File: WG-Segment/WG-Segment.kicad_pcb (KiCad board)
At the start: 4 copper layers, 100 x 100 mm, 137 parts, among them J101 Conn_01x02, J102 Conn_02x04_Odd_Even, J201 Conn_01x03, J202 Conn_01x02, J203 Conn_01x04, J501 Conn_01x02, J502 Conn_01x02, J503 Conn_01x02, J504 Conn_01x02, J505 Conn_01x02, J506 Conn_01x02, J507 Conn_01x02, J508 Conn_01x02, J509 Conn_01x02, J510 Conn_01x02, J511 Conn_01x02, J512 Conn_01x02, J513 Conn_01x02, J514 Conn_01x02, J515 Conn_01x02, J516 Conn_01x02, J517 Conn_01x02, J518 Conn_01x02, J519 Conn_01x02, J520 Conn_01x02, J521 Conn_01x02, J522 Conn_01x02, J523 Conn_01x02, J524 Conn_01x02, J525 Conn_01x02, SW201 SPST-NO, U201 W25Q16JV, U202 RP2040, U301 AP63205WU, U302 MIC5504-3.3YM5, U303 MCP1501T-33E, U401 SN74LV1T34DCK, U501 SN74LV4051ADYYR, U502 SN74LV4051ADYYR, U503 SN74LV4051ADYYR, U504 SN74LV4051ADYYR, Y201 12MHz

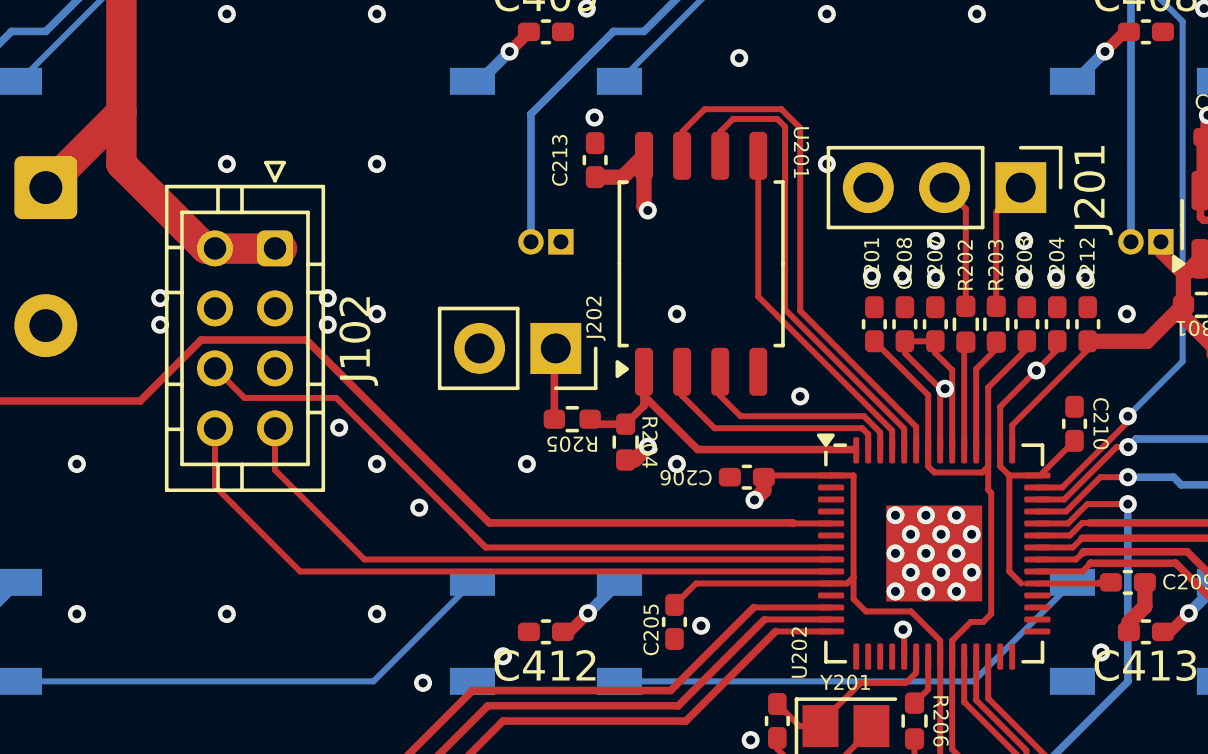
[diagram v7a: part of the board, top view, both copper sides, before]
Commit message: Minor pinout adjustments
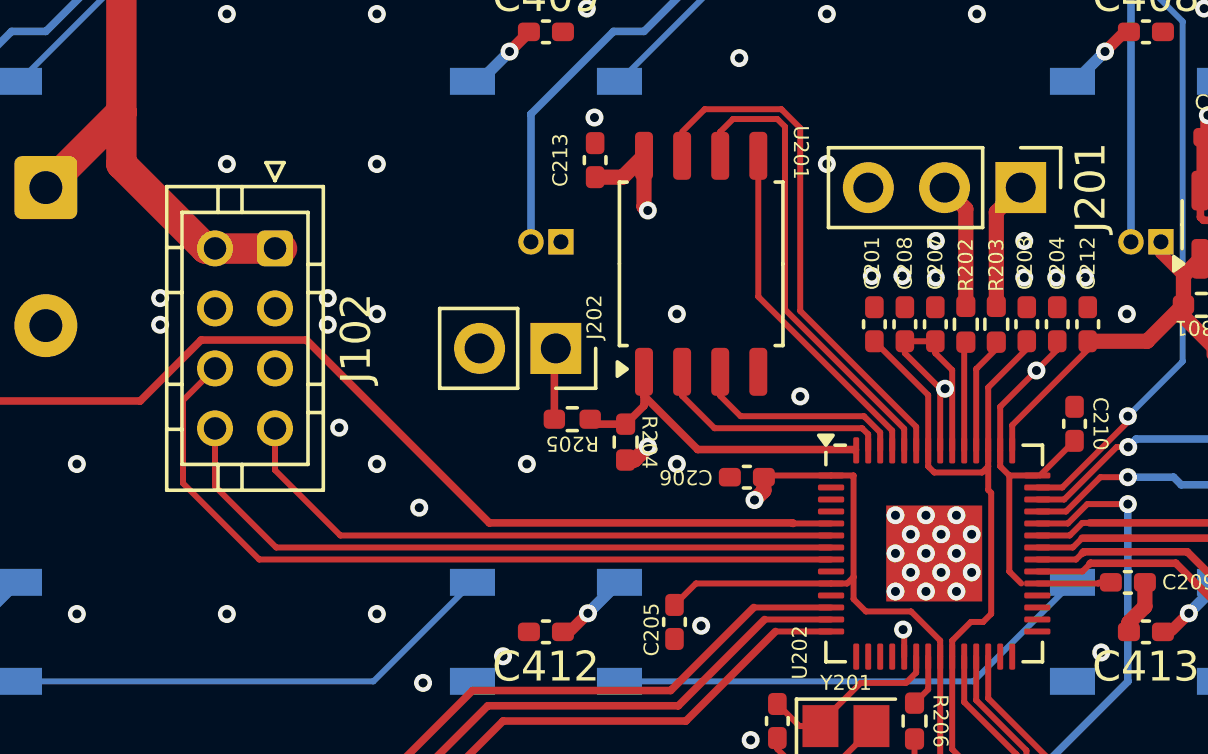
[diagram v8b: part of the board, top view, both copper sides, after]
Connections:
- U202 pad 6: unconnected-(U202-GPIO4-Pad6) -> /SDA
- U202 pad 7: /~{DS}/~{INT} -> /SCK
- U202 pad 8: /SDA -> /~{DS}/~{INT}
- U202 pad 9: /SCK -> unconnected-(U202-GPIO7-Pad9)
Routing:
- net /~{DS}/~{INT}: track 23.7 -> 26.9 mm
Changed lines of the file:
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@@
   (net 108 "unconnected-(U504-Y3-Pad12)")
   (net 109 "unconnected-(U202-GPIO21-Pad32)")
-  (net 110 "unconnected-(U202-GPIO4-Pad6)")
+  (net 110 "unconnected-(U202-GPIO7-Pad9)")
   (net 111 "unconnected-(U202-GPIO20-Pad31)")
   (net 112 "unconnected-(U202-GPIO19-Pad30)")
@@
       (net 85 "/CPU/LED_DOUT") (pinfunction "GPIO3") (pintype "bidirectional"))
     (pad "6" smd roundrect (at -3.4375 -0.6) (size 0.875 0.2) (layers "F.Cu" "F.Paste" "F.Mask") (roundrect_rratio 0.25)
-      (net 110 "unconnected-(U202-GPIO4-Pad6)") (pinfunction "GPIO4") (pintype "bidirectional+no_connect"))
+      (net 39 "/SDA") (pinfunction "GPIO4") (pintype "bidirectional"))
     (pad "7" smd roundrect (at -3.4375 -0.2) (size 0.875 0.2) (layers "F.Cu" "F.Paste" "F.Mask") (roundrect_rratio 0.25)
-      (net 38 "/~{DS}{slash}~{INT}") (pinfunction "GPIO5") (pintype "bidirectional"))
+      (net 40 "/SCK") (pinfunction "GPIO5") (pintype "bidirectional"))
     (pad "8" smd roundrect (at -3.4375 0.2) (size 0.875 0.2) (layers "F.Cu" "F.Paste" "F.Mask") (roundrect_rratio 0.25)
-      (net 39 "/SDA") (pinfunction "GPIO6") (pintype "bidirectional"))
+      (net 38 "/~{DS}{slash}~{INT}") (pinfunction "GPIO6") (pintype "bidirectional"))
     (pad "9" smd roundrect (at -3.4375 0.6) (size 0.875 0.2) (layers "F.Cu" "F.Paste" "F.Mask") (roundrect_rratio 0.25)
-      (net 40 "/SCK") (pinfunction "GPIO7") (pintype "bidirectional"))
+      (net 110 "unconnected-(U202-GPIO7-Pad9)") (pinfunction "GPIO7") (pintype "bidirectional+no_connect"))
     (pad "10" smd roundrect (at -3.4375 1) (size 0.875 0.2) (layers "F.Cu" "F.Paste" "F.Mask") (roundrect_rratio 0.25)
       (net 10 "+3V3") (pinfunction "IOVDD") (pintype "passive"))
@@
   (segment (start 181.41 139.77) (end 184.71 136.47) (width 0.2) (layer "B.Cu") (net 36))
   (segment (start 169.61 139.77) (end 181.41 139.77) (width 0.2) (layer "B.Cu") (net 36))
-  (segment (start 120.170928 90.3224) (end 117.1128 90.3224) (width 0.2) (layer "F.Cu") (net 38))
-  (segment (start 136.6645 95.3075) (end 125.156028 95.3075) (width 0.2) (layer "F.Cu") (net 38))
-  (segment (start 117.1128 90.3224) (end 117.094 90.3036) (width 0.2) (layer "F.Cu") (net 38))
-  (segment (start 125.156028 95.3075) (end 124.677664 94.829136) (width 0.2) (layer "F.Cu") (net 38))
-  (segment (start 125.149329 95.3008) (end 124.677664 94.829136) (width 0.2) (layer "F.Cu") (net 38))
-  (segment (start 117.094 90.3036) (end 116.1288 89.3384) (width 0.2) (layer "F.Cu") (net 38))
-  (segment (start 124.677664 94.829136) (end 120.170928 90.3224) (width 0.2) (layer "F.Cu") (net 38))
-  (segment (start 136.6645 95.7075) (end 121.1075 95.7075) (width 0.2) (layer "F.Cu") (net 39))
+  (segment (start 115.062 93.1672) (end 115.062 90.4052) (width 0.2) (layer "F.Cu") (net 38))
+  (segment (start 136.6645 95.7075) (end 117.6023 95.7075) (width 0.2) (layer "F.Cu") (net 38))
+  (segment (start 117.6023 95.7075) (end 115.062 93.1672) (width 0.2) (layer "F.Cu") (net 38))
+  (segment (start 115.062 90.4052) (end 116.1288 89.3384) (width 0.2) (layer "F.Cu") (net 38))
+  (segment (start 136.6645 94.9075) (end 120.3075 94.9075) (width 0.2) (layer "F.Cu") (net 39))
+  (segment (start 120.3075 94.9075) (end 118.1288 92.7288) (width 0.2) (layer "F.Cu") (net 39))
   (segment (start 118.1288 92.7288) (end 118.1288 91.3384) (width 0.2) (layer "F.Cu") (net 39))
-  (segment (start 121.1075 95.7075) (end 118.1288 92.7288) (width 0.2) (layer "F.Cu") (net 39))
-  (segment (start 136.6645 96.1075) (end 118.9675 96.1075) (width 0.2) (layer "F.Cu") (net 40))
-  (segment (start 118.9675 96.1075) (end 116.7384 93.8784) (width 0.2) (layer "F.Cu") (net 40))
+  (segment (start 118.1675 95.3075) (end 116.1288 93.2688) (width 0.2) (layer "F.Cu") (net 40))
   (segment (start 116.1288 93.2688) (end 116.1288 91.3384) (width 0.2) (layer "F.Cu") (net 40))
-  (segment (start 116.7384 93.8784) (end 116.1288 93.2688) (width 0.2) (layer "F.Cu") (net 40))
-  (segment (start 142.172 84.127) (end 142.172 87.2685) (width 0.2) (layer "F.Cu") (net 41))
-  (segment (start 142.987 83.312) (end 142.172 84.127) (width 0.2) (layer "F.Cu") (net 41))
-  (segment (start 141.156 84.021) (end 141.156 87.2685) (width 0.2) (layer "F.Cu") (net 42))
-  (segment (start 140.447 83.312) (end 141.156 84.021) (width 0.2) (layer "F.Cu") (net 42))
+  (segment (start 136.6645 95.3075) (end 118.1675 95.3075) (width 0.2) (layer "F.Cu") (net 40))
+  (segment (start 142.172 84.127) (end 142.172 87.2685) (width 0.508) (layer "F.Cu") (net 41))
+  (segment (start 142.987 83.312) (end 142.172 84.127) (width 0.508) (layer "F.Cu") (net 41))
+  (segment (start 141.156 84.021) (end 141.156 87.2685) (width 0.508) (layer "F.Cu") (net 42))
+  (segment (start 140.447 83.312) (end 141.156 84.021) (width 0.508) (layer "F.Cu") (net 42))
   (segment (start 127.4405 91.032) (end 127.4405 88.7905) (width 0.254) (layer "F.Cu") (net 43))
   (segment (start 141.102 100.462) (end 141.102 98.945) (width 0.2) (layer "F.Cu") (net 44))
@@
   (segment (start 135.009448 80.699) (end 135.636 81.325552) (width 0.2) (layer "F.Cu") (net 84))
   (segment (start 115.667112 88.392) (end 113.635112 90.424) (width 0.254) (layer "F.Cu") (net 85))
-  (segment (start 119.1768 88.392) (end 115.667112 88.392) (width 0.254) (layer "F.Cu") (net 85))
-  (segment (start 113.635112 90.424) (end 102.616 90.424) (width 0.254) (layer "F.Cu") (net 85))
-  (segment (start 136.6645 94.5075) (end 135.4015 94.5075) (width 0.2) (layer "F.Cu") (net 85))
   (segment (start 102.616 90.424) (end 100.65525 88.46325) (width 0.254) (layer "F.Cu") (net 85))
-  (segment (start 125.2728 94.488) (end 119.1768 88.392) (width 0.254) (layer "F.Cu") (net 85))
   (segment (start 135.382 94.488) (end 125.2728 94.488) (width 0.254) (layer "F.Cu") (net 85))
   (segment (start 100.65525 88.46325) (end 100.65525 69.361536) (width 0.254) (layer "F.Cu") (net 85))
+  (segment (start 125.2728 94.488) (end 119.1768 88.392) (width 0.254) (layer "F.Cu") (net 85))
+  (segment (start 136.6645 94.5075) (end 135.4015 94.5075) (width 0.2) (layer "F.Cu") (net 85))
+  (segment (start 119.1768 88.392) (end 115.667112 88.392) (width 0.254) (layer "F.Cu") (net 85))
+  (segment (start 113.635112 90.424) (end 102.616 90.424) (width 0.254) (layer "F.Cu") (net 85))
   (segment (start 135.4015 94.5075) (end 135.382 94.488) (width 0.254) (layer "F.Cu") (net 85))
   (segment (start 137.541 73.533) (end 136.41 72.402) (width 0.254) (layer "F.Cu") (net 93))
@@
     (members
       03359038-6afb-49c8-89ea-c871b5d0dea5
-      08f9dd6d-e438-448d-88e2-5aceae488f64
       0d7081e5-3a9d-4e1e-bdf7-4b5c83120a9a
       0dddea51-cb82-4ace-b283-61c5c85605a8
@@
       5c8af1ad-f158-4644-88a3-53d484ebecf9
       5df6fc83-64e3-4012-beb3-e788afee01c7
+      69c0d572-e73a-404f-a1b2-4b984d082031
+      6ecfccfb-bbe3-464d-b8e4-69134661479e
       725fb274-fcab-4d65-83d1-7a8ff9b37af9
       7fd90004-76d7-4225-9db1-5ded9cc999a1
@@
       8607276a-7543-4cd4-80aa-ee77bf82eff9
       881c5a37-861d-496b-9a74-cd1fe81aeb10
+      8c90c014-23f6-4647-889e-ae22c5bdd1de
       8d05e33c-2cc9-413d-9108-33a4526be501
       93bbaa32-9ea4-4185-a147-862f39192aab
